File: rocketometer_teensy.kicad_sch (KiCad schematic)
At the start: 3 parts, among them J101 Teensy4.1, J102 STANDOFF, J103 STANDOFF

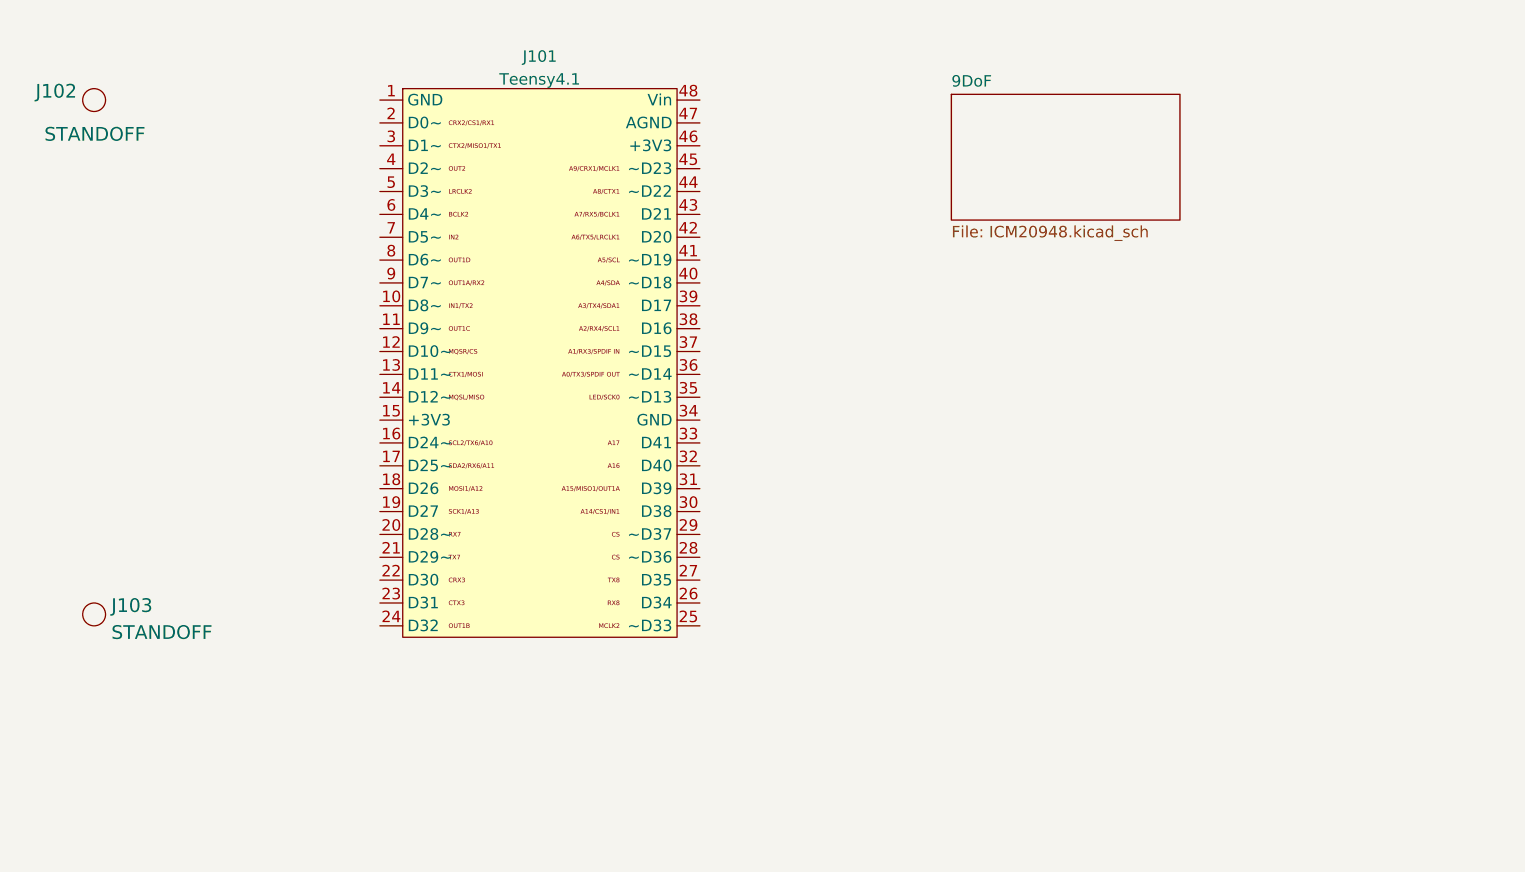
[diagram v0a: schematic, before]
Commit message: Moved ICM-20948 schematic to kwan_kicad_lib
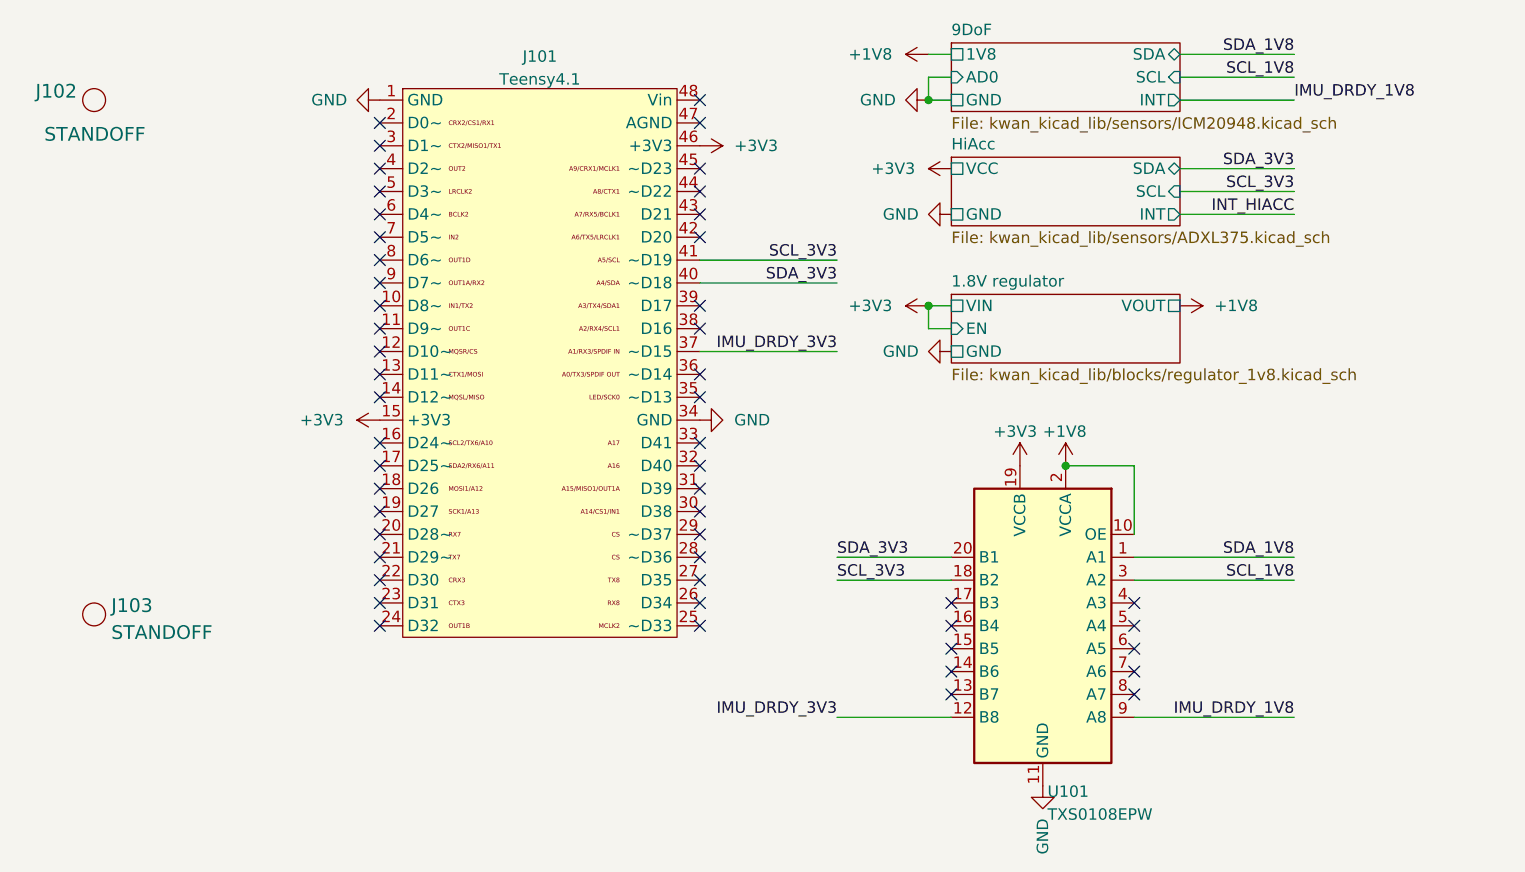
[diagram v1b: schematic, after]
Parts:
- added U101: TXS0108EPW, Package_SO:TSSOP-20_4.4x6.5mm_P0.65mm, symbol Logic_LevelTranslator:TXS0108EPW
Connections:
- net GND: now reaches J101.1 (GND)
- net GND: now also J101.34 (GND), U101.11 (GND)
- net +3V3: now reaches J101.15 (+3V3)
- net +3V3: now also J101.46 (+3V3), U101.19 (VCCB)
- net IMU_DRDY_3V3: now reaches J101.37 (~D15)
- net IMU_DRDY_3V3: now also U101.12 (B8)
- net SDA_3V3: now reaches J101.40 (~D18)
- net SDA_3V3: now also U101.20 (B1)
- net SCL_3V3: now reaches J101.41 (~D19)
- net SCL_3V3: now also U101.18 (B2)
- new net +1V8: U101.10 (OE), U101.2 (VCCA)
- new net IMU_DRDY_1V8: U101.9 (A8)
- new net SCL_1V8: U101.3 (A2)
- new net SDA_1V8: U101.1 (A1)
- no-connect marks 0 -> 51
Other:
- added sheet 1.8V regulator (kwan_kicad_lib/blocks/regulator_1v8.kicad_sch)
- added sheet HiAcc (kwan_kicad_lib/sensors/ADXL375.kicad_sch)
- sheet 9DoF: file ICM20948.kicad_sch -> kwan_kicad_lib/sensors/ICM20948.kicad_sch
- sheet 9DoF ports: added 1V8, AD0, GND, INT, SCL, SDA; removed none
